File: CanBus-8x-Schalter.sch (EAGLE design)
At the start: 67 parts, among them IC1 LM2937IMP-5.0, IC2 ATMEGA1284P, IC3 MCP2515T-I/SO, IC4 MCP2562-E/SN, K1 36.11, K2 36.11, K3 36.11, K4 36.11, K5 36.11, K6 36.11, K7 36.11, K8 36.11, Q1 EUROQUARTZ-MMJ, Q2 EUROQUARTZ-MMJ, X1 MKDSN1,5/3-5,08, X2 MKDSN1,5/3-5,08, X3 MKDSN1,5/3-5,08, X4 MKDSN1,5/3-5,08, X5 MKDSN1,5/3-5,08, X6 MKDSN1,5/3-5,08, X7 MKDSN1,5/3-5,08, X8 MKDSN1,5/3-5,08

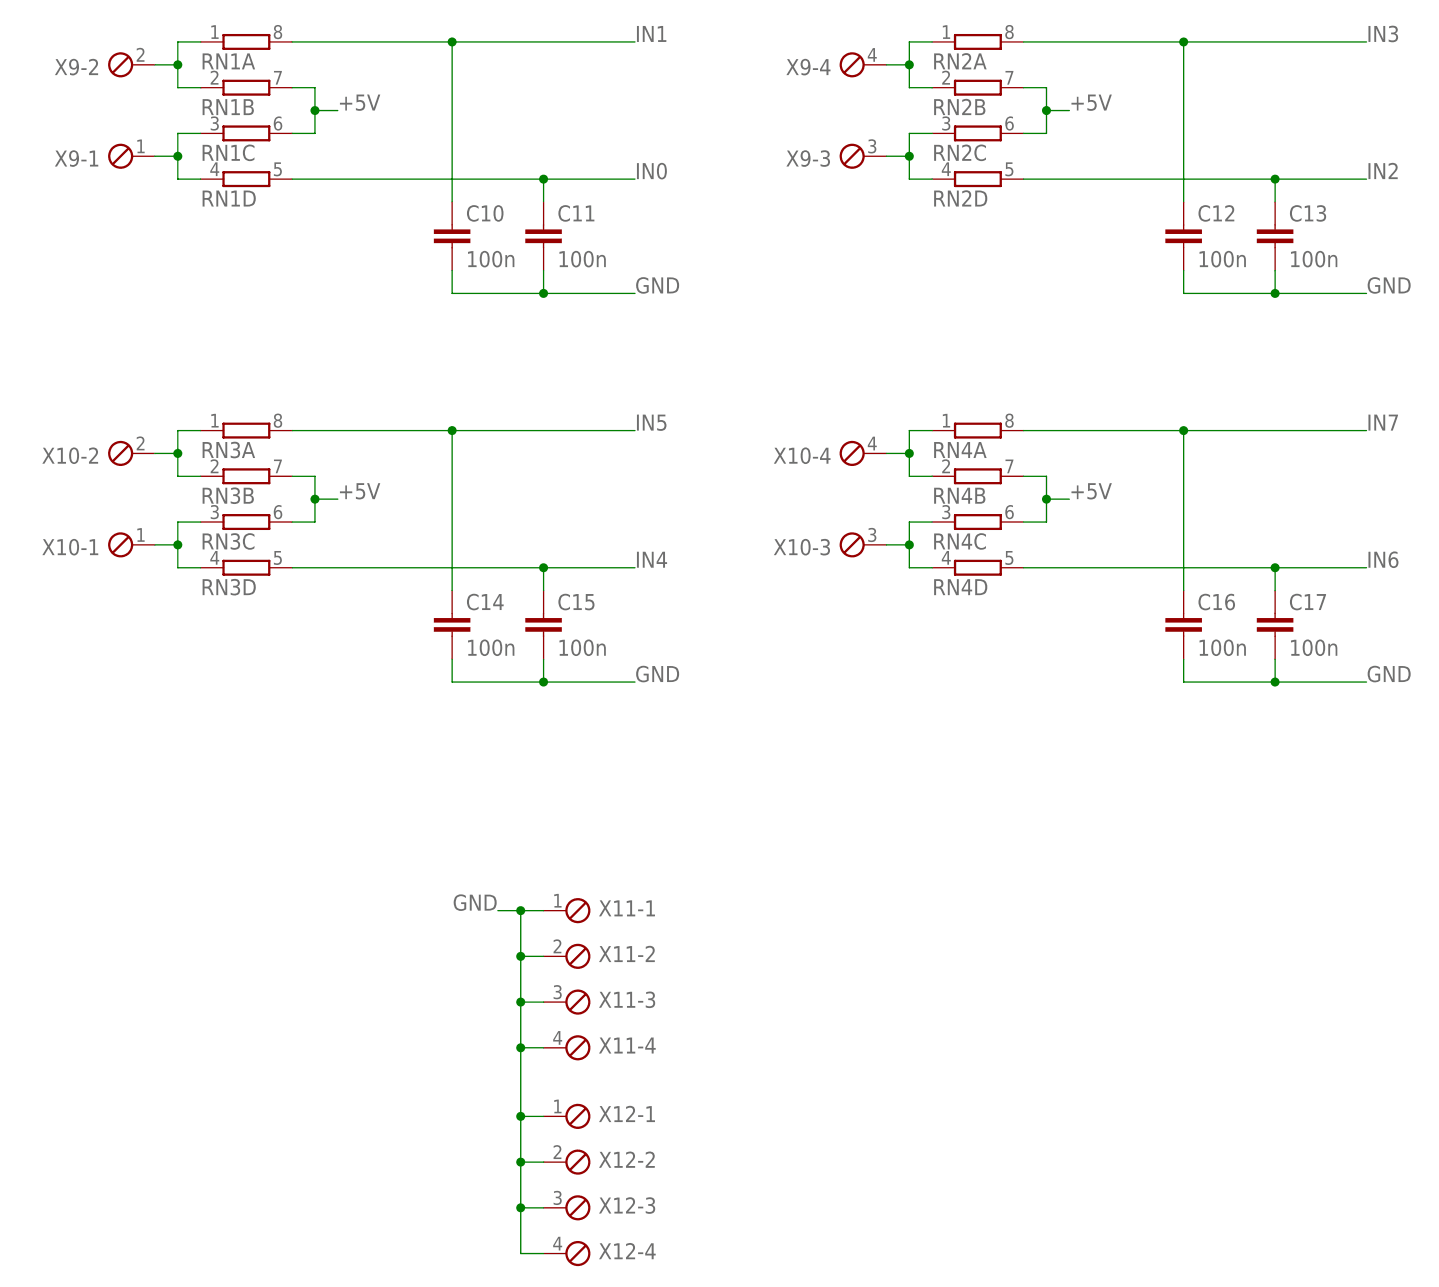
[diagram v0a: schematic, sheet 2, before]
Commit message: Werte von Bauteilen angepasst
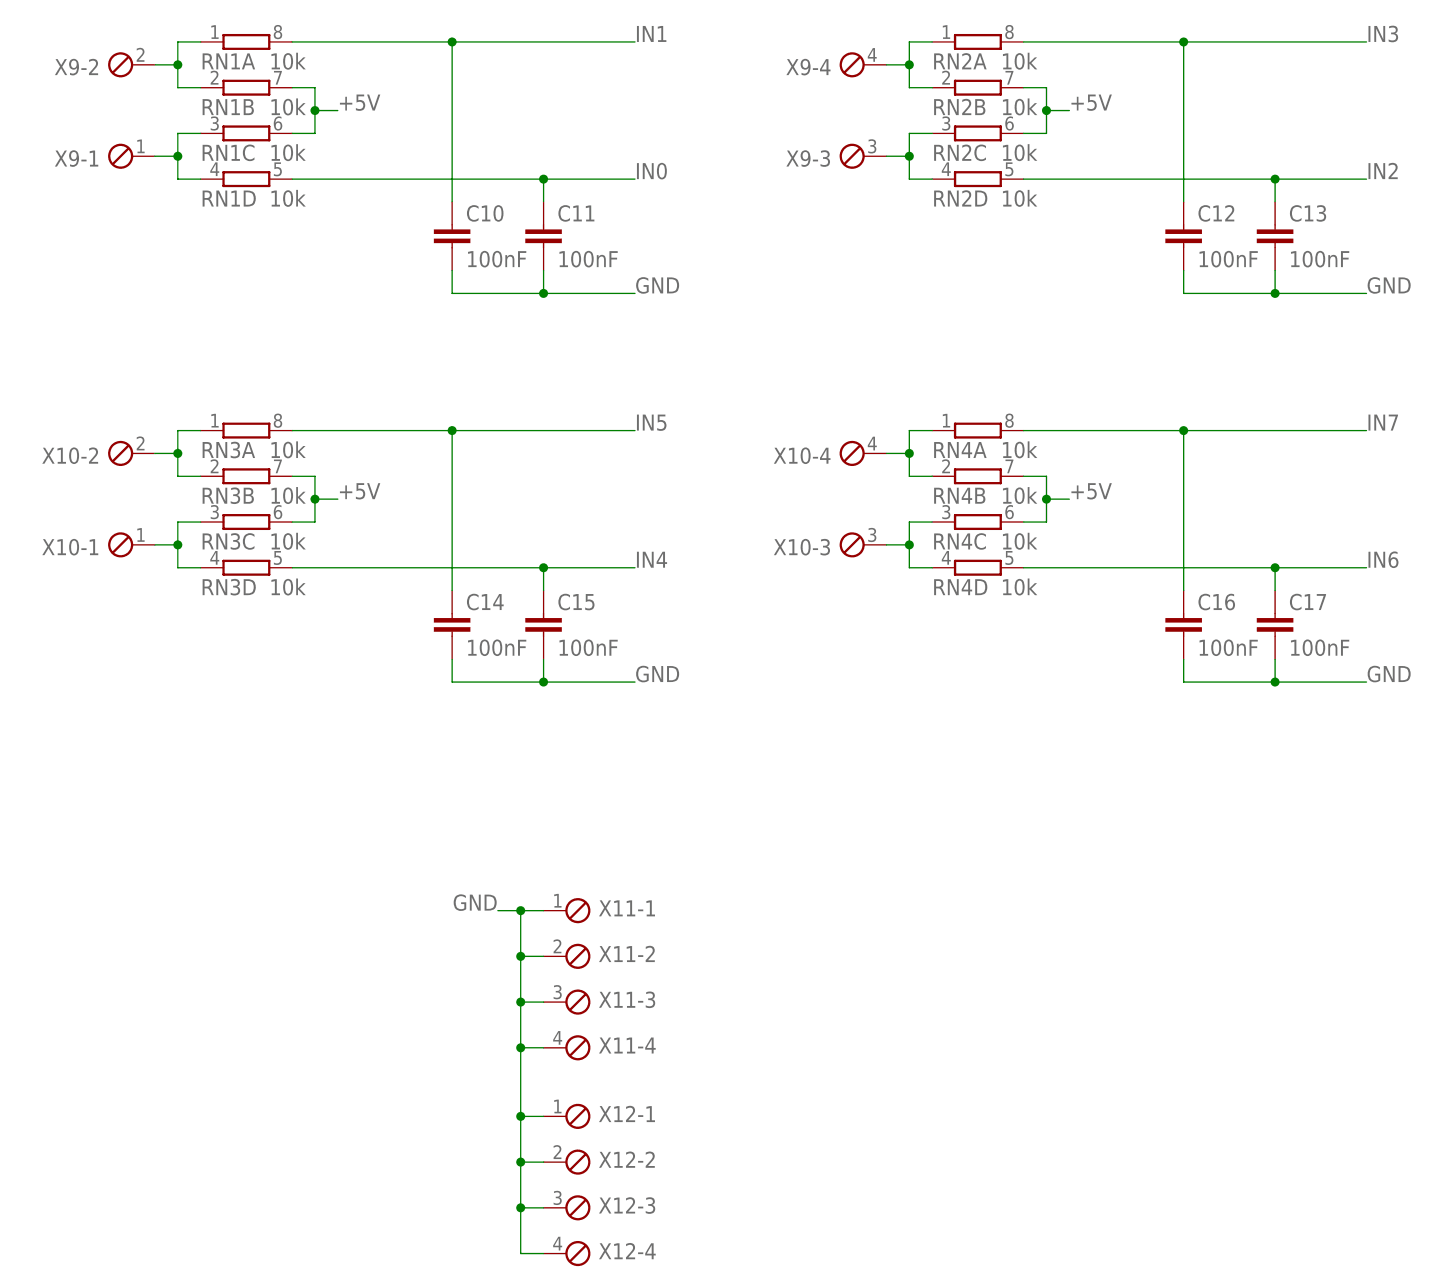
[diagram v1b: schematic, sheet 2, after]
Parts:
- C1: value (none) -> 100nF
- C10, C11, C12, C13, C14, C15, C16, C17: value 100n -> 100nF
- C2: value (none) -> 10µF Low ESR
- Q1, Q2: value EUROQUARTZ-MMJ -> 16MHz
- RN1, RN2, RN3, RN4: value (none) -> 10k
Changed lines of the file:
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@@
 <parts>
 <part name="IC1" library="lm2937" deviceset="LM2937IMP-*" device="" technology="5.0"/>
-<part name="C1" library="rcl" deviceset="C-EU" device="C0805"/>
-<part name="C2" library="rcl" deviceset="C-EU" device="C0805"/>
+<part name="C1" library="rcl" deviceset="C-EU" device="C0805" value="100nF"/>
+<part name="C2" library="rcl" deviceset="C-EU" device="C0805" value="10µF Low ESR"/>
 <part name="IC3" library="mcp2515_2551_2562" deviceset="MCP2515" device="T-I/SO"/>
 <part name="IC4" library="mcp2515_2551_2562" deviceset="MCP2562" device="-E/SN"/>
-<part name="Q1" library="crystal-smd" deviceset="EUROQUARTZ-M*" device="MJ"/>
+<part name="Q1" library="crystal-smd" deviceset="EUROQUARTZ-M*" device="MJ" value="16MHz"/>
 <part name="C3" library="rcl" deviceset="C-EU" device="C0805" value="22pF"/>
 <part name="C4" library="rcl" deviceset="C-EU" device="C0805" value="22pF"/>
-<part name="Q2" library="crystal-smd" deviceset="EUROQUARTZ-M*" device="MJ"/>
+<part name="Q2" library="crystal-smd" deviceset="EUROQUARTZ-M*" device="MJ" value="16MHz"/>
 <part name="C5" library="rcl" deviceset="C-EU" device="C0805" value="22pF"/>
 <part name="C6" library="rcl" deviceset="C-EU" device="C0805" value="22pF"/>
@@
 <part name="C9" library="rcl" deviceset="C-EU" device="C0805" value="100nF"/>
 <part name="R2" library="rcl" deviceset="R-EU_" device="R0805" value="4k7"/>
-<part name="RN1" library="resistor-dil" deviceset="4R-N" device="0603-ARC"/>
-<part name="C10" library="rcl" deviceset="C-EU" device="C0805" value="100n"/>
-<part name="C11" library="rcl" deviceset="C-EU" device="C0805" value="100n"/>
+<part name="RN1" library="resistor-dil" deviceset="4R-N" device="0603-ARC" value="10k"/>
+<part name="C10" library="rcl" deviceset="C-EU" device="C0805" value="100nF"/>
+<part name="C11" library="rcl" deviceset="C-EU" device="C0805" value="100nF"/>
 <part name="SDA" library="solpad" deviceset="LSP13" device=""/>
 <part name="SCL" library="solpad" deviceset="LSP13" device=""/>
@@
 <part name="K4" library="relay_finder_36_11" deviceset="36.11" device=""/>
 <part name="X4" library="con-phoenix-508" deviceset="MKDSN1,5/3-5,08" device=""/>
-<part name="RN2" library="resistor-dil" deviceset="4R-N" device="0603-ARC"/>
-<part name="C12" library="rcl" deviceset="C-EU" device="C0805" value="100n"/>
-<part name="C13" library="rcl" deviceset="C-EU" device="C0805" value="100n"/>
+<part name="RN2" library="resistor-dil" deviceset="4R-N" device="0603-ARC" value="10k"/>
+<part name="C12" library="rcl" deviceset="C-EU" device="C0805" value="100nF"/>
+<part name="C13" library="rcl" deviceset="C-EU" device="C0805" value="100nF"/>
 <part name="J1" library="can-bus" deviceset="RJ45-CAN" device=""/>
 <part name="K5" library="relay_finder_36_11" deviceset="36.11" device=""/>
@@
 <part name="IC5" library="uln-udn" deviceset="ULN2803A" device="-SO18W"/>
 <part name="FRAME3" library="frames" deviceset="A4L-LOC" device=""/>
-<part name="RN3" library="resistor-dil" deviceset="4R-N" device="0603-ARC"/>
-<part name="C14" library="rcl" deviceset="C-EU" device="C0805" value="100n"/>
-<part name="C15" library="rcl" deviceset="C-EU" device="C0805" value="100n"/>
-<part name="RN4" library="resistor-dil" deviceset="4R-N" device="0603-ARC"/>
-<part name="C16" library="rcl" deviceset="C-EU" device="C0805" value="100n"/>
-<part name="C17" library="rcl" deviceset="C-EU" device="C0805" value="100n"/>
+<part name="RN3" library="resistor-dil" deviceset="4R-N" device="0603-ARC" value="10k"/>
+<part name="C14" library="rcl" deviceset="C-EU" device="C0805" value="100nF"/>
+<part name="C15" library="rcl" deviceset="C-EU" device="C0805" value="100nF"/>
+<part name="RN4" library="resistor-dil" deviceset="4R-N" device="0603-ARC" value="10k"/>
+<part name="C16" library="rcl" deviceset="C-EU" device="C0805" value="100nF"/>
+<part name="C17" library="rcl" deviceset="C-EU" device="C0805" value="100nF"/>
 <part name="X9" library="con-phoenix-254" deviceset="MPT4" device=""/>
 <part name="X10" library="con-phoenix-254" deviceset="MPT4" device=""/>

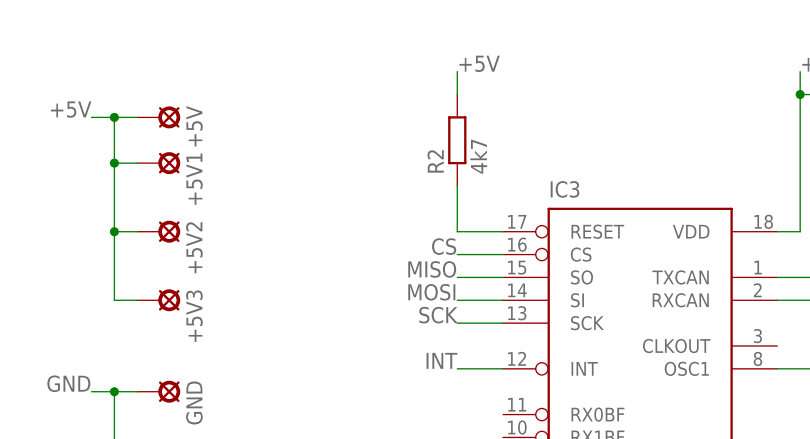
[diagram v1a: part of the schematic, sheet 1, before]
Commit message: CAN-Bus 8x-Schalter CS PullUp hinzugefügt
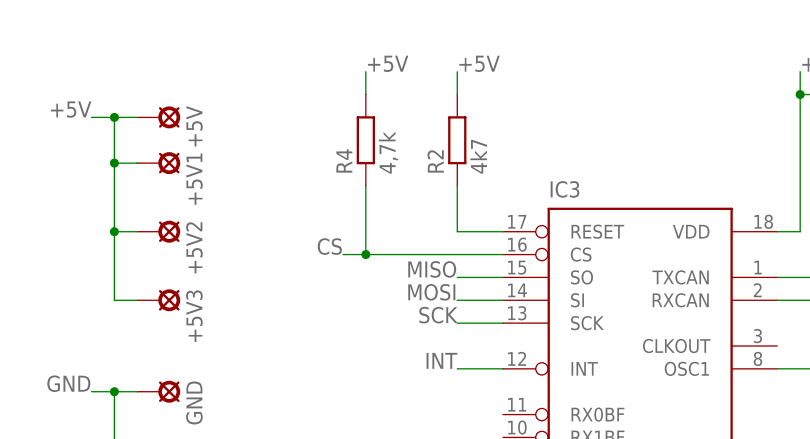
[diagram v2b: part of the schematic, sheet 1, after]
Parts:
- added R4: 4,7k, rcl:R-EU_R0805
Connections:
- net +5V: now also R4.2
- net CS: now also R4.1
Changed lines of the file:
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@@
 <?xml version="1.0" encoding="utf-8"?>
 <!DOCTYPE eagle SYSTEM "eagle.dtd">
-<eagle version="7.4.0">
+<eagle version="7.7.0">
 <drawing>
 <settings>
@@
 <part name="R3" library="rcl" deviceset="R-EU_" device="R0805" value="1k2"/>
 <part name="LED1" library="led" deviceset="LED" device="CHIPLED_1206" value="2mA bl"/>
+<part name="R4" library="rcl" deviceset="R-EU_" device="R0805" value="4,7k"/>
 </parts>
 <sheets>
@@
 <instance part="R3" gate="G$1" x="127" y="58.42"/>
 <instance part="LED1" gate="G$1" x="137.16" y="58.42" rot="R90"/>
+<instance part="R4" gate="G$1" x="162.56" y="157.48" rot="R90"/>
 </instances>
 <busses>
@@
 <junction x="193.04" y="53.34"/>
 <label x="195.58" y="53.34" size="1.778" layer="95"/>
+</segment>
+<segment>
+<pinref part="R4" gate="G$1" pin="2"/>
+<wire x1="162.56" y1="162.56" x2="162.56" y2="165.1" width="0.1524" layer="91"/>
+<label x="162.56" y="165.1" size="1.778" layer="95"/>
 </segment>
 </net>
@@
 <segment>
 <pinref part="IC3" gate="G$1" pin="CS"/>
-<wire x1="172.72" y1="144.78" x2="177.8" y2="144.78" width="0.1524" layer="91"/>
-<label x="172.72" y="144.78" size="1.778" layer="95" rot="MR0"/>
-</segment>
-<segment>
+<wire x1="160.02" y1="144.78" x2="162.56" y2="144.78" width="0.1524" layer="91"/>
+<label x="160.02" y="144.78" size="1.778" layer="95" rot="MR0"/>
+<pinref part="R4" gate="G$1" pin="1"/>
+<wire x1="162.56" y1="144.78" x2="177.8" y2="144.78" width="0.1524" layer="91"/>
+<wire x1="162.56" y1="152.4" x2="162.56" y2="144.78" width="0.1524" layer="91"/>
+<junction x="162.56" y="144.78"/>
+</segment>
+<segment>
